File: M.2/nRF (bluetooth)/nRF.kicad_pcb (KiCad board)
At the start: 2 copper layers, 22 x 4 mm, 1 part

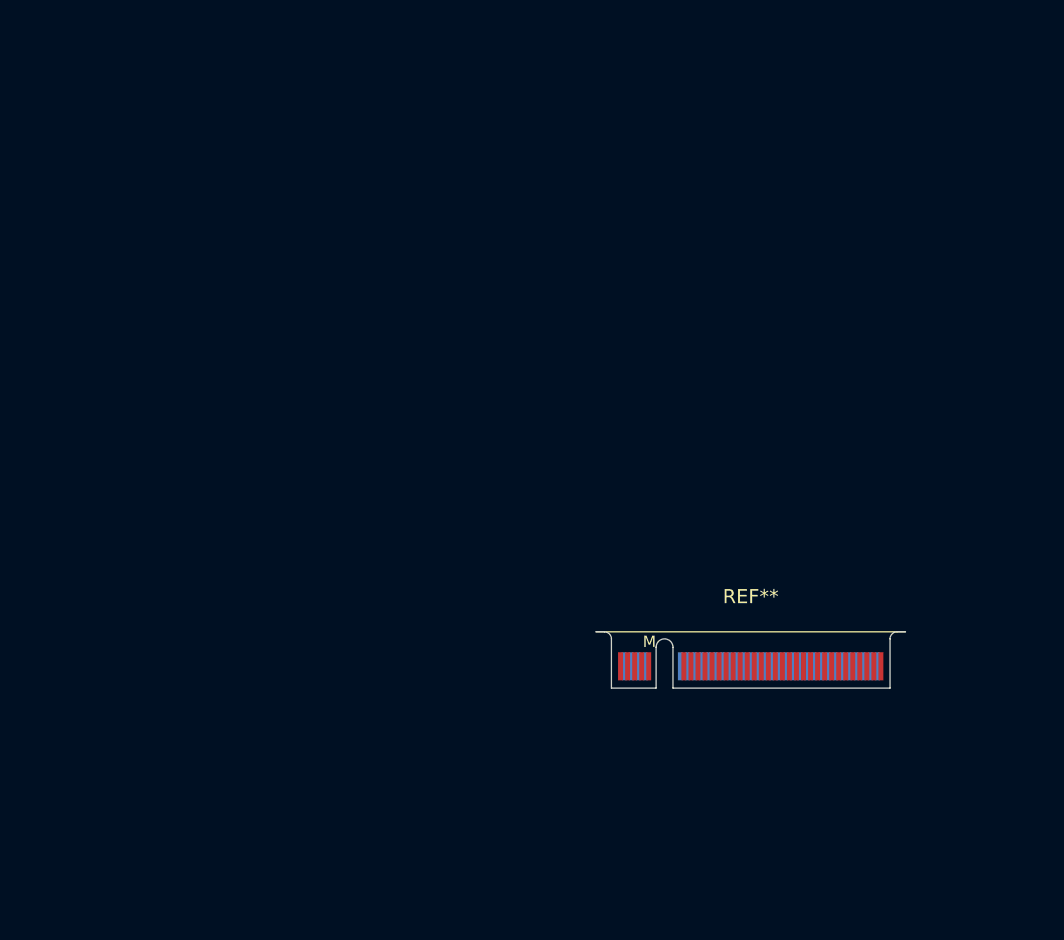
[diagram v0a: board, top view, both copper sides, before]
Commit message: add bluetooth m.2 carrier schematics and accompanying things
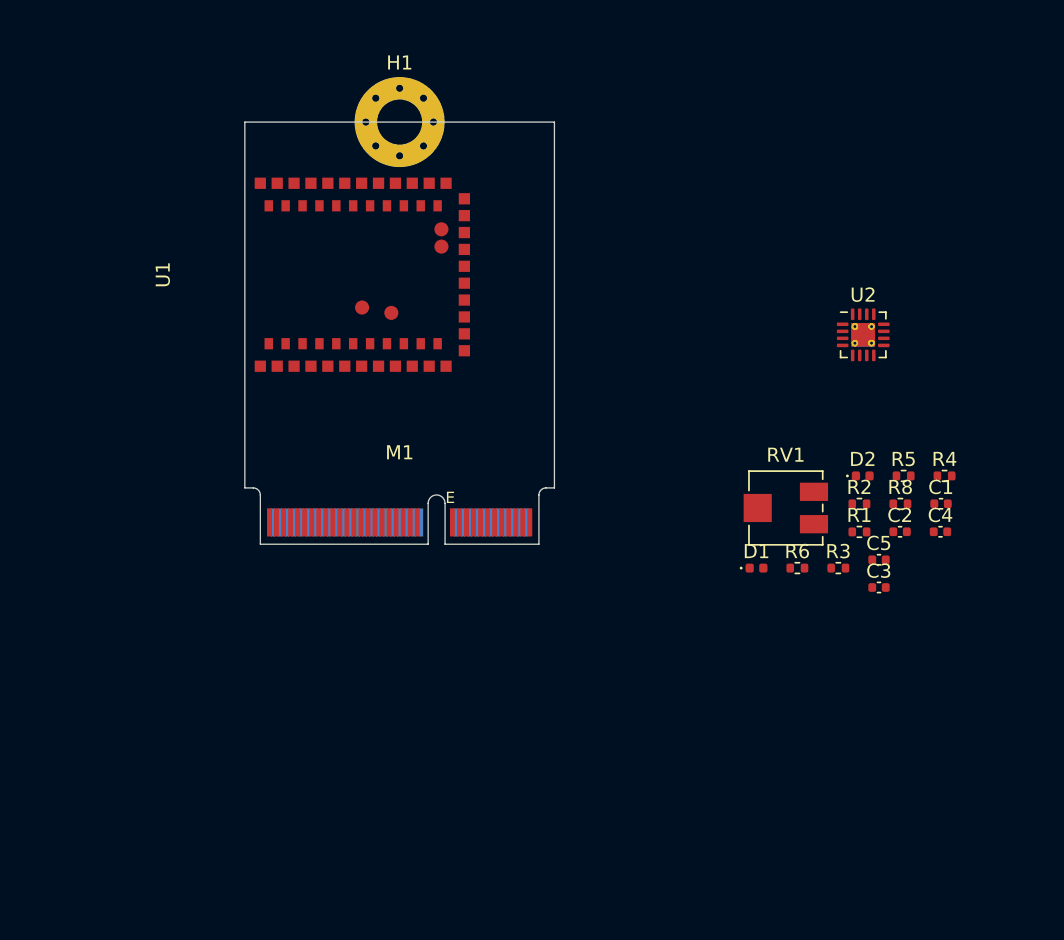
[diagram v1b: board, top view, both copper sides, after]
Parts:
- removed REF**: m2-padKeyM, m2ngff:m2-padKeyM
- added C1: 4.7u, Capacitor_SMD:C_0402_1005Metric, F.Cu at (49.5, 27.1)
- added C2: 4.7u, Capacitor_SMD:C_0402_1005Metric, F.Cu at (46.6, 29.1)
- added C3: 1u, Capacitor_SMD:C_0402_1005Metric, F.Cu at (45.1, 33.1)
- added C4: 1u, Capacitor_SMD:C_0402_1005Metric, F.Cu at (49.4, 29.1)
- added C5: 4.7u, Capacitor_SMD:C_0402_1005Metric, F.Cu at (45.1, 31.1)
- added D1: LED, LED_SMD:LED_0402_1005Metric, F.Cu at (36.4, 31.7)
- added D2: LED, LED_SMD:LED_0402_1005Metric, F.Cu at (43.9, 25.1)
- added H1: MountingHole_Pad, MountingHole:MountingHole_3.2mm_M3_Pad_Via, F.Cu at (11.0, 0.00)
- added M1: M.2_Key_E, m2ngff:m2-padKeyE, F.Cu at (11.0, 30.0)
- added R1: 820K, Resistor_SMD:R_0402_1005Metric, F.Cu at (43.7, 29.1)
- added R2: 2M, Resistor_SMD:R_0402_1005Metric, F.Cu at (43.7, 27.1)
- added R3: 1.5k, Resistor_SMD:R_0402_1005Metric, F.Cu at (42.2, 31.7)
- added R4: 1.5k, Resistor_SMD:R_0402_1005Metric, F.Cu at (49.7, 25.1)
- added R5: 10k, Resistor_SMD:R_0402_1005Metric, F.Cu at (46.8, 25.1)
- added R6: R_TMR, Resistor_SMD:R_0402_1005Metric, F.Cu at (39.3, 31.7)
- added R8: R_ITERM, Resistor_SMD:R_0402_1005Metric, F.Cu at (46.6, 27.1)
- added RV1: R_Potentiometer_Trim, Potentiometer_SMD:Potentiometer_Vishay_TS53YJ_Vertical, F.Cu at (38.4, 27.4)
- added U1: MK08, moko:MK08, F.Cu at (5.50, 10.8)
- added U2: BQ24232HARGTT, Package_DFN_QFN:VQFN-16-1EP_3x3mm_P0.5mm_EP1.68x1.68mm_ThermalVias, F.Cu at (43.9, 15.1)
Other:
- board size 22 x 4 mm -> 22 x 26 mm

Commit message: last touchups to nRF
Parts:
- added L1: TapTap Logo, LogoSmall:tt_4mm, F.Cu at (18.4, 2.77)
- added SW101: RESET, LogoSmall:LogoSmall, F.Cu at (3.90, 2.40)
- R6, R8: footprint Resistor_SMD:R_0402_1005Metric -> Capacitor_SMD:C_0402_1005Metric
- moved C2 36.2 mm to (11.4, 20.6), turned to 180 degrees
- moved C1 35.7 mm to (19.3, 8.10), turned to 90 degrees
- moved R8 34.9 mm to (19.2, 5.53)
- moved R6 32.2 mm to (19.2, 6.53)
- moved R4 31.9 mm to (17.9, 23.4), turned to -90 degrees
- moved C4 31.7 mm to (20.0, 17.2)
- moved R5 31.0 mm to (16.9, 16.9), turned to -90 degrees
- moved R2 30.0 mm to (14.2, 21.4), turned to -90 degrees
- moved C5 29.4 mm to (16.7, 23.4), turned to -90 degrees
- moved R1 29.4 mm to (15.3, 21.4), turned to 90 degrees
- moved C3 26.8 mm to (21.0, 21.2), turned to -90 degrees
- moved U2 26.1 mm to (18.3, 20.0)
- moved D2 25.0 mm to (18.9, 23.4), turned to -90 degrees
- moved RV1 24.6 mm to (19.0, 12.4), turned to -90 degrees
- moved R3 22.6 mm to (21.1, 23.4), turned to -90 degrees
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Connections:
- C1 pad 2: Net-(U1-Pad43) -> GND
- C2 pad 1: Net-(U1-Pad43) -> GND
- M1 pad 10: +3V3 -> VDD
- M1 pad 32: unconnected-(M1-Pad32) -> P17
- M1 pad 33: unconnected-(M1-Pad33) -> P7
- M1 pad 34: unconnected-(M1-Pad34) -> P18
- M1 pad 35: unconnected-(M1-Pad35) -> P6
- M1 pad 36: unconnected-(M1-Pad36) -> P19
- M1 pad 37: unconnected-(M1-Pad37) -> P5
- M1 pad 38: unconnected-(M1-Pad38) -> P20
- M1 pad 39: unconnected-(M1-Pad39) -> P4
- M1 pad 4: +3V3 -> GND
- M1 pad 40: unconnected-(M1-Pad40) -> P37
- M1 pad 41: unconnected-(M1-Pad41) -> P3
- M1 pad 42: unconnected-(M1-Pad42) -> P21
- M1 pad 43: unconnected-(M1-Pad43) -> P2
- M1 pad 44: unconnected-(M1-Pad44) -> P38
- M1 pad 45: unconnected-(M1-Pad45) -> P1
- M1 pad 46: unconnected-(M1-Pad46) -> P22
- M1 pad 47: unconnected-(M1-Pad47) -> P0
- M1 pad 48: unconnected-(M1-Pad48) -> P39
- M1 pad 49: unconnected-(M1-Pad49) -> P28
- M1 pad 50: unconnected-(M1-Pad50) -> P23
- M1 pad 51: unconnected-(M1-Pad51) -> P29
- M1 pad 52: unconnected-(M1-Pad52) -> P24
- M1 pad 53: unconnected-(M1-Pad53) -> P30
- M1 pad 54: unconnected-(M1-Pad54) -> P25
- M1 pad 55: unconnected-(M1-Pad55) -> P31
- M1 pad 56: unconnected-(M1-Pad56) -> P26
- M1 pad 57: unconnected-(M1-Pad57) -> P43
- M1 pad 58: unconnected-(M1-Pad58) -> P27
- M1 pad 59: unconnected-(M1-Pad59) -> P42
- M1 pad 9: +3V3 -> VDD
- U1 pad 1: unconnected-(U1-Pad1) -> P0
- U1 pad 10: Net-(U1-Pad43) -> GND
- U1 pad 11: unconnected-(U1-Pad11) -> P8
- U1 pad 12: unconnected-(U1-Pad12) -> P9
- U1 pad 14: unconnected-(U1-Pad14) -> P10
- U1 pad 15: unconnected-(U1-Pad15) -> P11
- U1 pad 16: unconnected-(U1-Pad16) -> P12
- U1 pad 17: unconnected-(U1-Pad17) -> P13
- U1 pad 18: unconnected-(U1-Pad18) -> P14
- U1 pad 2: unconnected-(U1-Pad2) -> P1
- U1 pad 21: unconnected-(U1-Pad21) -> P15
- U1 pad 22: unconnected-(U1-Pad22) -> P16
- U1 pad 23: unconnected-(U1-Pad23) -> P17
- U1 pad 24: unconnected-(U1-Pad24) -> P18
- U1 pad 25: unconnected-(U1-Pad25) -> P19
- U1 pad 26: unconnected-(U1-Pad26) -> P20
- U1 pad 28: unconnected-(U1-Pad28) -> P21
- U1 pad 29: unconnected-(U1-Pad29) -> P22
- U1 pad 3: unconnected-(U1-Pad3) -> P2
- U1 pad 30: unconnected-(U1-Pad30) -> P23
- U1 pad 31: unconnected-(U1-Pad31) -> P24
- U1 pad 32: unconnected-(U1-Pad32) -> P25
- U1 pad 33: unconnected-(U1-Pad33) -> P26
- U1 pad 34: unconnected-(U1-Pad34) -> P27
- U1 pad 35: unconnected-(U1-Pad35) -> P28
- U1 pad 36: unconnected-(U1-Pad36) -> P29
- U1 pad 37: unconnected-(U1-Pad37) -> P30
- U1 pad 38: unconnected-(U1-Pad38) -> P31
- U1 pad 39: Net-(U1-Pad43) -> GND
- U1 pad 4: unconnected-(U1-Pad4) -> P3
- U1 pad 40: unconnected-(U1-Pad40) -> P32
- U1 pad 41: unconnected-(U1-Pad41) -> P33
- U1 pad 43: Net-(U1-Pad43) -> GND
- U1 pad 44: unconnected-(U1-Pad44) -> P34
- U1 pad 45: unconnected-(U1-Pad45) -> P35
- U1 pad 49: unconnected-(U1-Pad49) -> P36
- U1 pad 5: unconnected-(U1-Pad5) -> P4
- U1 pad 50: unconnected-(U1-Pad50) -> P37
- U1 pad 51: unconnected-(U1-Pad51) -> P38
- U1 pad 52: unconnected-(U1-Pad52) -> P39
- U1 pad 53: unconnected-(U1-Pad53) -> P40
- U1 pad 54: unconnected-(U1-Pad54) -> P41
- U1 pad 55: unconnected-(U1-Pad55) -> P42
- U1 pad 56: unconnected-(U1-Pad56) -> P43
- U1 pad 57: Net-(U1-Pad43) -> GND
- U1 pad 6: unconnected-(U1-Pad6) -> P5
- U1 pad 7: unconnected-(U1-Pad7) -> P6
- U1 pad 8: unconnected-(U1-Pad8) -> P7
- U1 pad 9: unconnected-(U1-Pad9) -> VDD
- U2 pad 17: (no net) -> GND
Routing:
- net GND: track 0.00 -> 52.0 mm, vias 0 -> 16
- net reset: track 0.00 -> 41.1 mm, vias 0 -> 1
- net vddh: track 0.00 -> 33.4 mm, vias 0 -> 4
- net +5V: track 0.00 -> 31.6 mm, vias 0 -> 3
- net swdclk: track 0.00 -> 29.1 mm, vias 0 -> 1
- net P17: track 0.00 -> 26.9 mm, vias 0 -> 1
- net swdio: track 0.00 -> 26.6 mm, vias 0 -> 1
- net USB-D-: track 0.00 -> 26.5 mm, vias 0 -> 1
- net P18: track 0.00 -> 25.9 mm, vias 0 -> 1
- net P19: track 0.00 -> 25.5 mm, vias 0 -> 1
- net USB-D+: track 0.00 -> 25.4 mm, vias 0 -> 1
- net P20: track 0.00 -> 25.2 mm, vias 0 -> 1
- net P27: track 0.00 -> 25.2 mm, vias 0 -> 1
- net P26: track 0.00 -> 24.9 mm, vias 0 -> 1
- net P25: track 0.00 -> 24.6 mm, vias 0 -> 1
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- added copper zone on B.Cu, net GND
- added copper zone on F.Cu, net GND
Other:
- board text added: "MUD Project M.2 Carrierboard nRF Edition Designed by Pat"

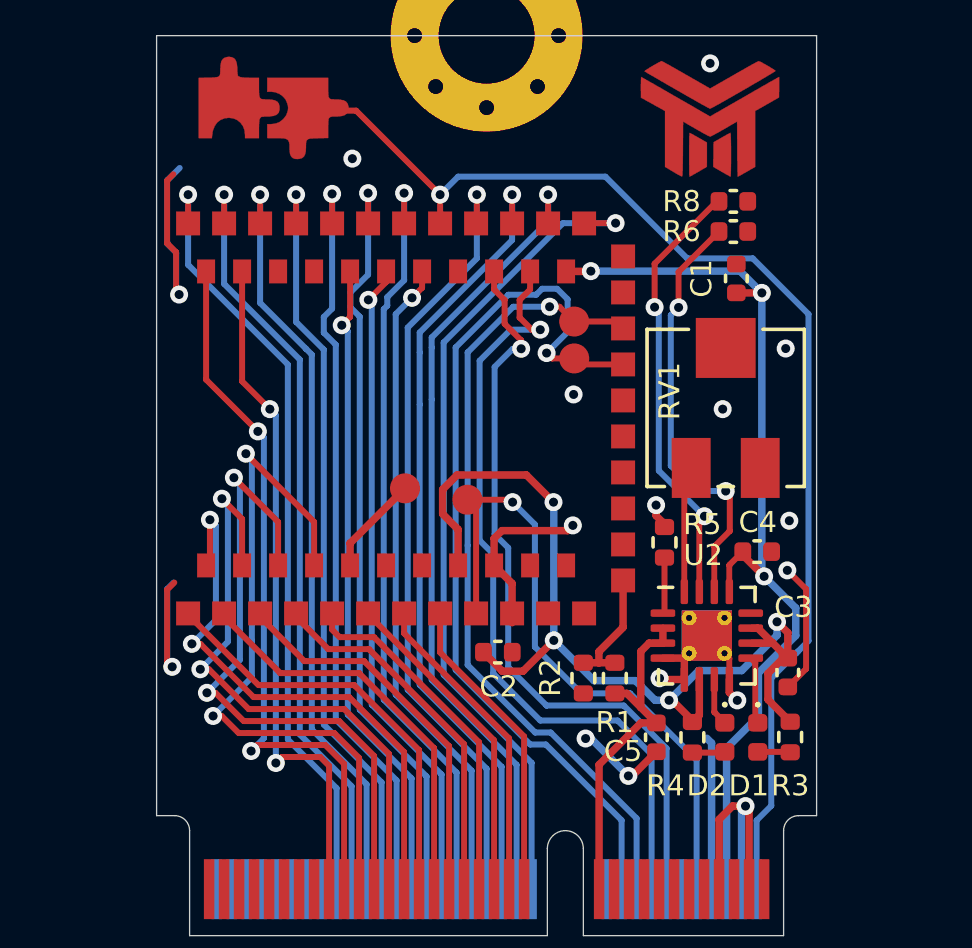
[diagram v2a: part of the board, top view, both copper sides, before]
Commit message: add teardrops to nrf
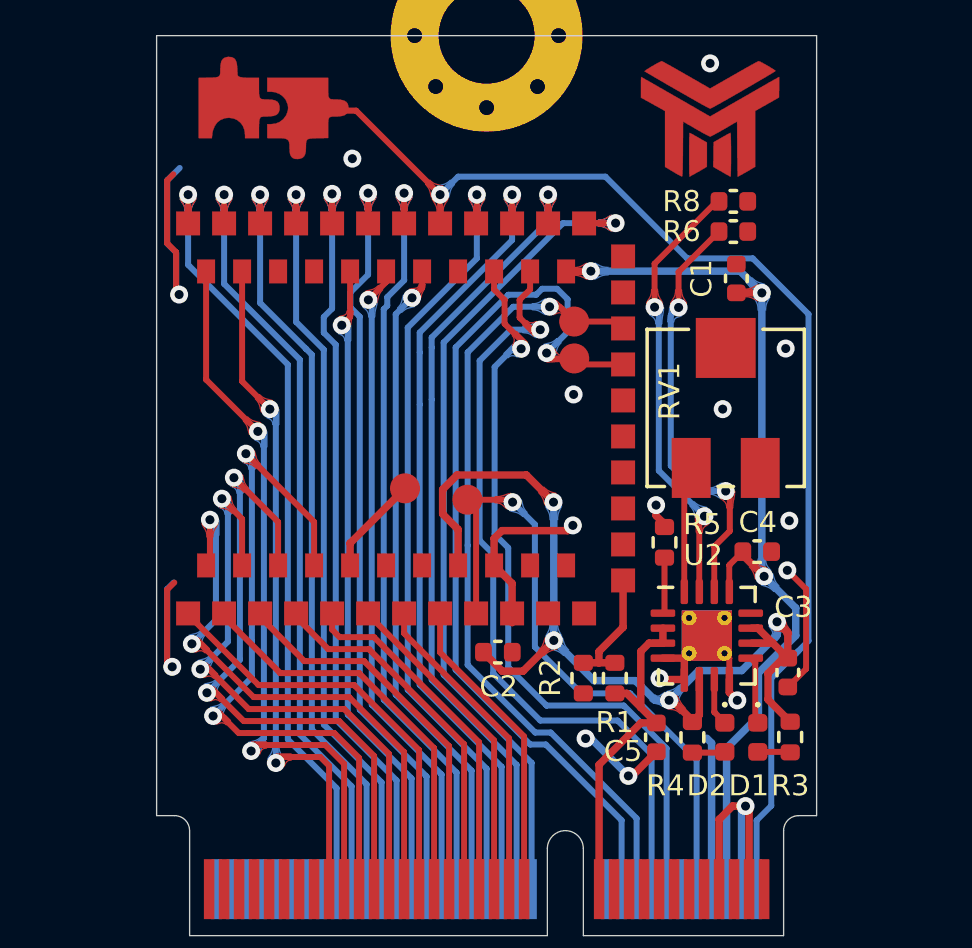
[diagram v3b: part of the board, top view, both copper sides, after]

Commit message: change vout on nRF to system out from the powerpath
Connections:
- M1 pad 10: VDD -> vddh
- M1 pad 9: VDD -> vddh
- U1 pad 9: VDD -> unconnected-(U1-Pad9)
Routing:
- net VDD: track 21.8 -> 0.00 mm, vias 1 -> 0
- net vddh: track 33.4 -> 35.9 mm
- net GND: track 52.0 -> 51.8 mm, vias 16 -> 18

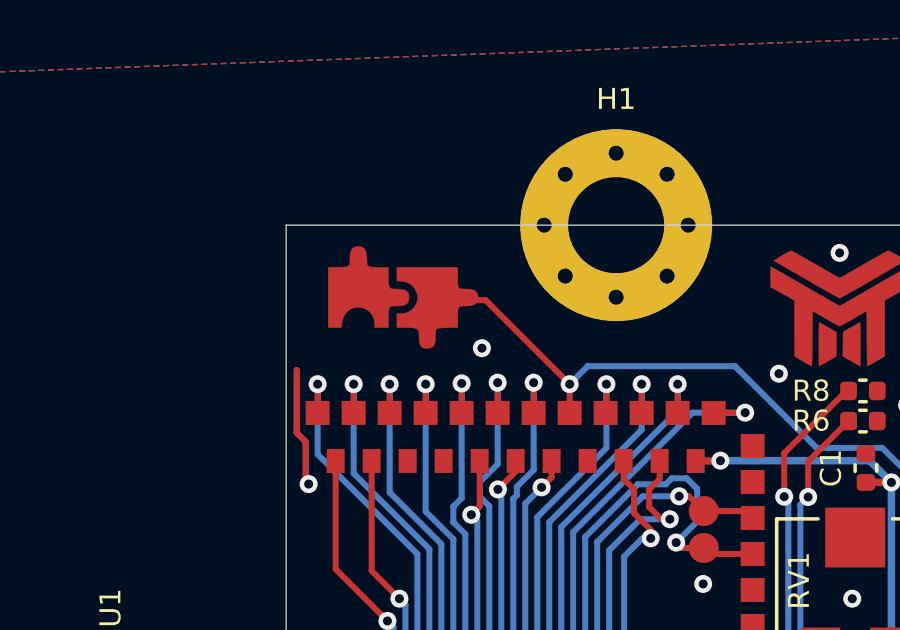
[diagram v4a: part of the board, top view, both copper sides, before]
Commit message: change modules to new logo
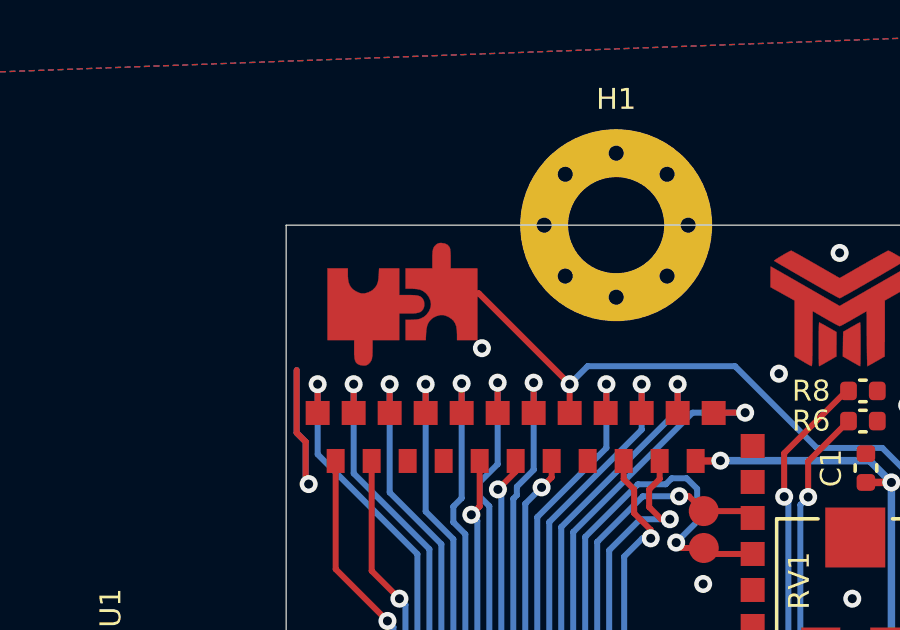
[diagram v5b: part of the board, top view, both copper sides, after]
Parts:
- SW101: footprint LogoSmall:LogoSmall -> LogoSmall:LogoSmall_Cu
- moved SW101 0.23 mm to (3.88, 2.62)
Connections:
- SW101 pad 1: reset -> GND
- SW101 pad 2: GND -> reset
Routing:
- net reset: track 41.0 -> 40.4 mm

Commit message: prettify files a lil bit
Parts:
- moved L1 30.4 mm to (42.2, 21.8)
- moved R3 30.4 mm to (44.9, 42.4)
- moved C2 30.4 mm to (35.1, 39.6)
- moved C3 30.4 mm to (44.8, 40.3)
- moved C4 30.4 mm to (43.8, 36.2)
- moved D1 30.4 mm to (43.8, 42.4)
- moved H1 30.4 mm to (34.8, 19.0)
- moved M1 30.4 mm to (34.8, 49.0)
- moved R1 30.4 mm to (39.0, 40.4)
- moved R2 30.4 mm to (38.0, 40.4)
- moved R4 30.4 mm to (41.6, 42.4)
- moved R5 30.4 mm to (40.7, 35.9)
- moved R8 30.4 mm to (43.0, 24.6)
- moved RV1 30.4 mm to (42.7, 31.4)
- moved SW101 30.4 mm to (27.6, 21.6)
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
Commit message: change up logo's to nicer ones on modules, update iss
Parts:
- added Ref**: Val**, silk:text, B.Cu at (34.8, 32.7)
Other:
- board text removed: "MUD Project M.2 Carrierboard nRF Edition Designed by Pat"
